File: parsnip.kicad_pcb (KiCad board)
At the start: 4 copper layers, 60 x 130 mm, 455 parts, among them J1 SPI BUS, J10 SOLAR, J11 Conn_Coaxial, J12 Conn_Coaxial_Small, J13 Conn_Coaxial, J14 GPIO_Expander, J15 LED 5V, J2 I2C3, J3 I2C1, J4 I2C2, J5 e-Ink Display Connector, J6 UART0, J7 GCT USB4105-GF-A-120, J8 PD_I2C DEBUG, J9 BAT_PORT, Q1 CSD25480F3, Q10 SI2308, Q11 CSD17581Q3A, Q12 AO3401A, Q13 BSS138, Q14 2N7002, Q15 2N7002, Q2 CSD15380F3, Q3 CSD25480F3, Q4 CSD15380F3, Q5 AON7534, Q6 AON7534, Q7 CSD18512Q5B, Q8 CSD18512Q5B, Q9 SI2308, SW1 ESP_RESET, SW2 BOOT, SW3 POWER/RESET, SW4 RESET_GNSS, SW5 SAFEBOOT_GNSS, U1 ESP32-S3-WROOM-1-N16R8, U10 TPS7A2033PDBVR, U11 TPS259474LRPWR, U12 E22P-915M30S, U13 LM61460AASQRJRRQ1, U14 LM61460AASQRJRRQ1, U15 TPS259474ARPWR, U16 SN74LVC1G74, U17 TCAL9539RTWR, U18 WS2816B, U19 SN74LV1T34DCK, U2 QMC6309, U20 WS2816B, U3 TVS2200DRV, U4 TPD8S300/A, U5 TI TPS25751DREFR, U6 CAT24C256, U7 MAX17320G22+, U8 BQ25798, U9 NEO-M9N, Y1 32.768KHz, Y2 SX1M4.000M10F30TNN

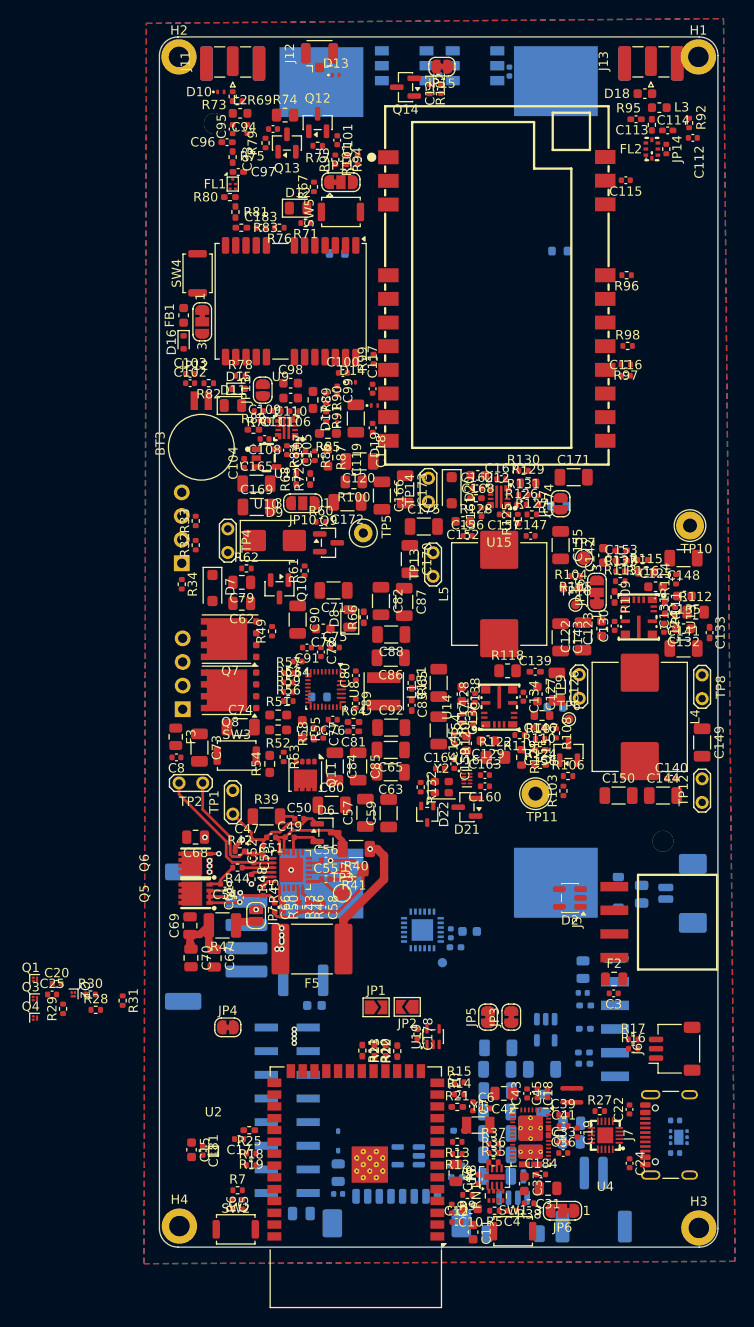
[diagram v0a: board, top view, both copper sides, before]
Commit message: slightly better component placement
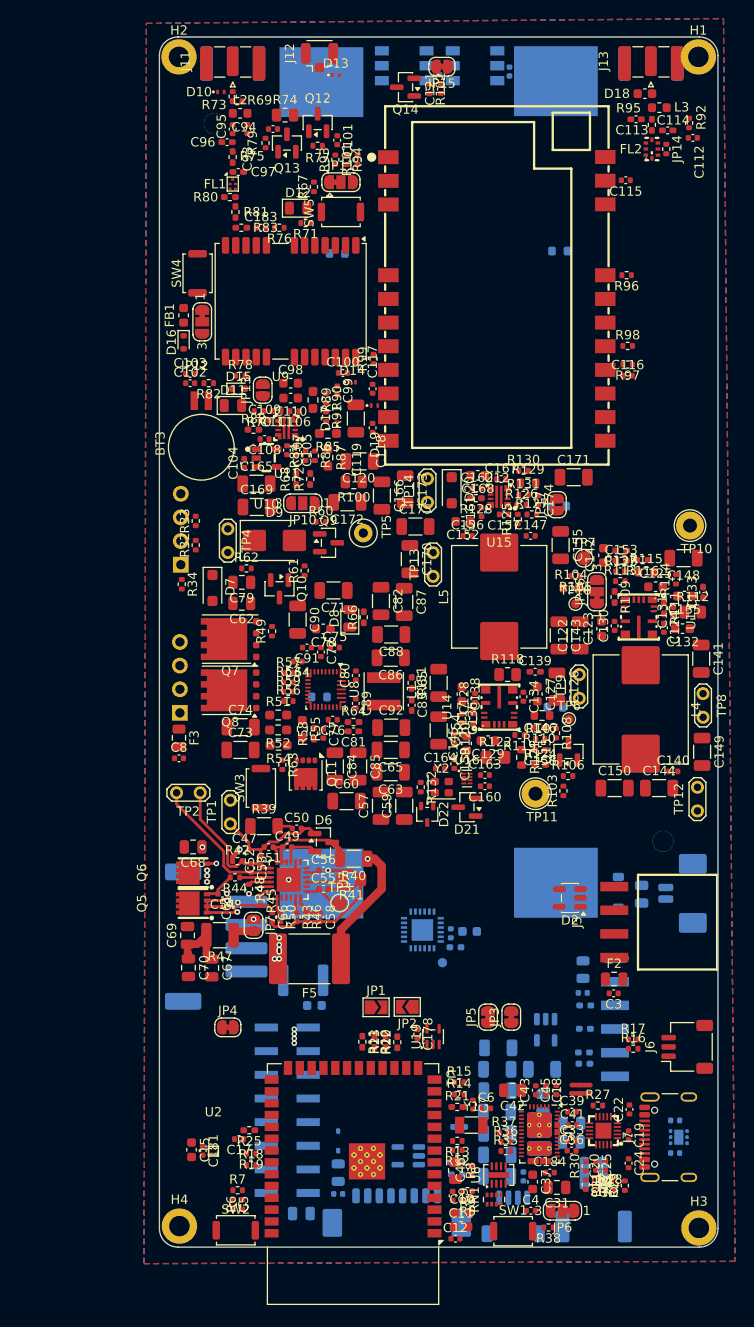
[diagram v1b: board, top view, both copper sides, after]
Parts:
- moved Q1 65.0 mm to (143.8, 158.1), turned to 180 degrees
- moved R29 63.3 mm to (145.8, 158.7)
- moved Q3 63.2 mm to (142.7, 158.1), turned to 180 degrees
- moved Q4 62.9 mm to (142.7, 159.1), turned to -90 degrees
- moved C20 62.1 mm to (143.8, 156.6), turned to 90 degrees
- moved Q2 61.5 mm to (144.8, 158.1), turned to 90 degrees
- moved C25 61.3 mm to (142.8, 156.5), turned to -90 degrees
- moved R28 58.5 mm to (144.2, 159.2)
- moved R30 56.3 mm to (141.7, 156.6), turned to 90 degrees
- moved R31 53.5 mm to (141.7, 158.6)
- moved C19 5.51 mm to (146.2, 153.2)
- moved C73 4.41 mm to (104.5, 111.8), turned to 0 degrees
- moved C133 4.39 mm to (154.2, 94.9), turned to 90 degrees
- moved SW3 4.36 mm to (106.8, 116.0), turned to 90 degrees
- moved R38 3.34 mm to (137.7, 163.2)
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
